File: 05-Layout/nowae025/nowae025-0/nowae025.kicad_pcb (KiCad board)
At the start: 2 copper layers, 17 parts, among them J1 JUMPER-2, J10 JUMPER-2, J11 JUMPER-2, J12 JUMPER-2, J13 JUMPER-2, J14 JUMPER-2, J2 JUMPER-2, J3 JUMPER-2, J4 JUMPER-2, J5 JUMPER-2, J6 JUMPER-2, J7 JUMPER-2, J8 JUMPER-2, J9 JUMPER-2, U1 BGM111A256V2

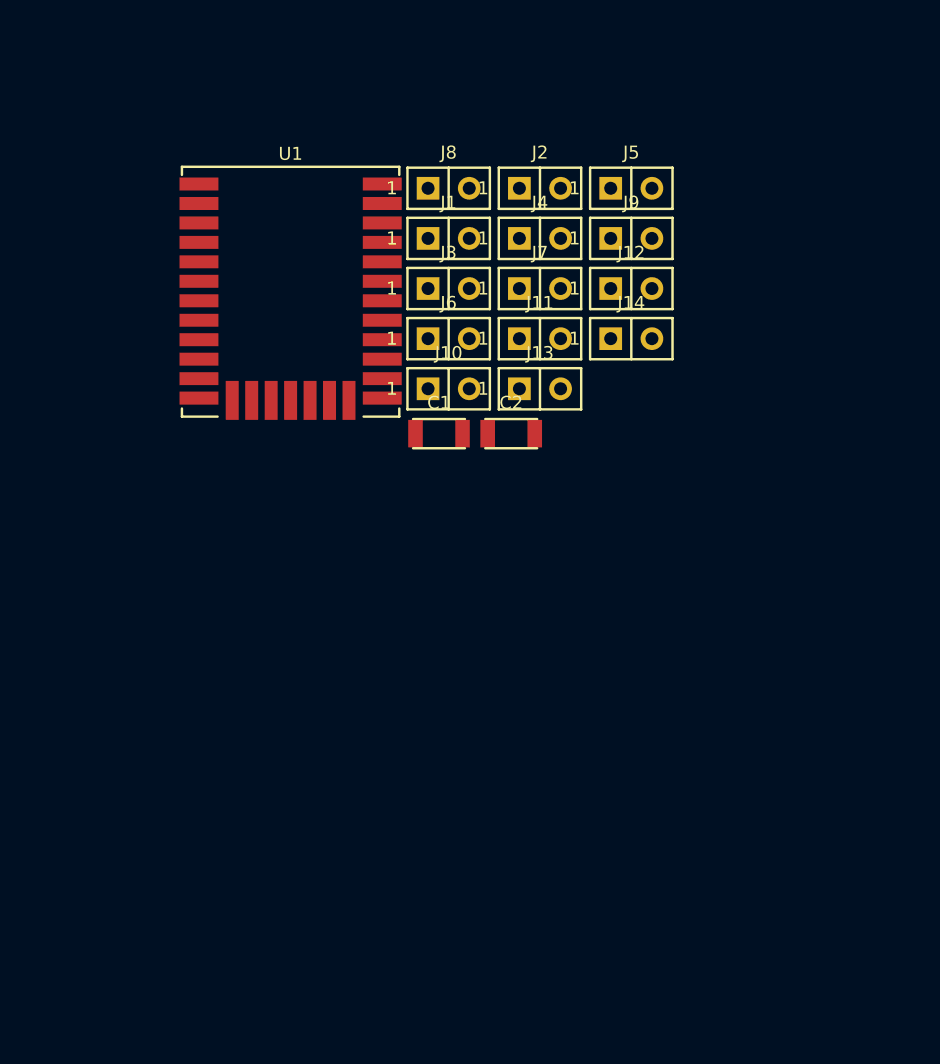
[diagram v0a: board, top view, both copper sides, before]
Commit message: Added missing footprint. Started component placement (nowae025)
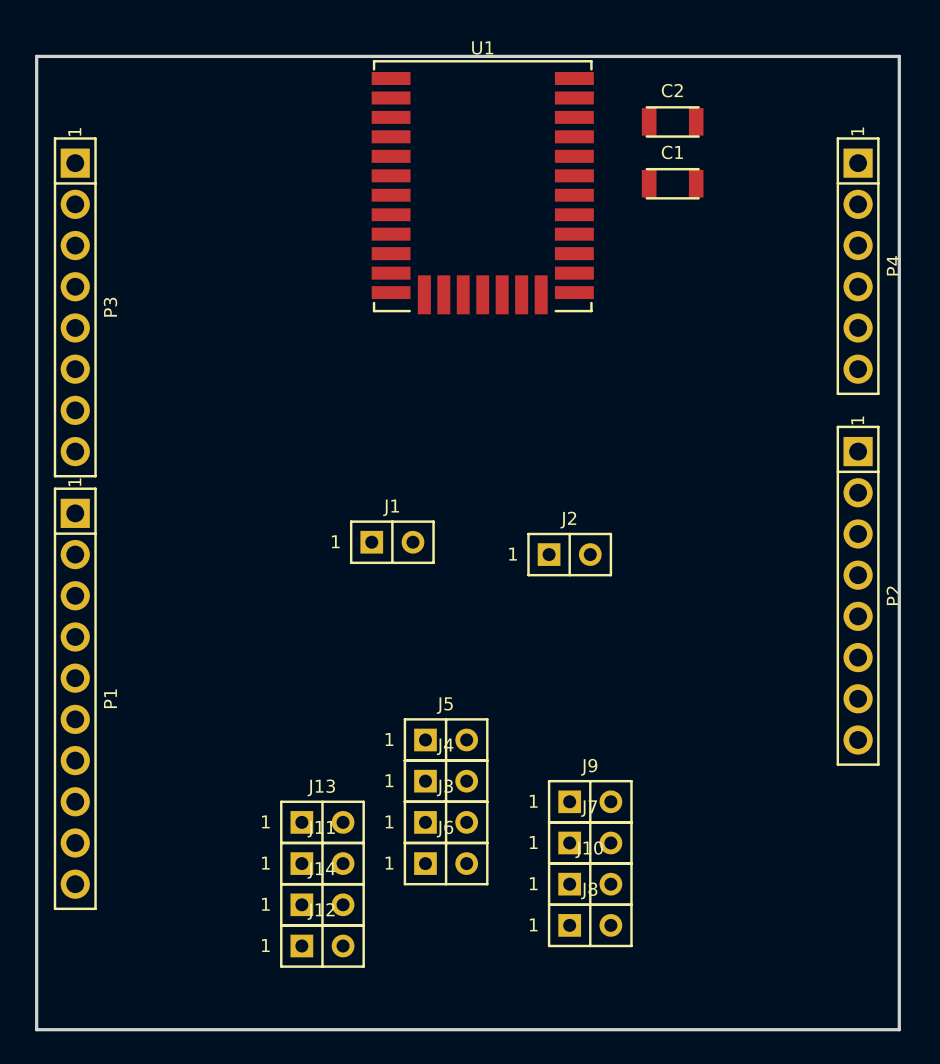
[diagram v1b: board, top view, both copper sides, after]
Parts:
- added P1: ARD_RIGHT2, CONNECTOR:SOCKET_10x1_2.54_WE-61301011821, F.Cu at (119.4, 101.6)
- added P2: ARD_LEFT2, CONNECTOR:SOCKET_8x1_2.54_WE-61300811821, F.Cu at (167.6, 95.2)
- added P3: ARD_RIGHT1, CONNECTOR:SOCKET_8x1_2.54_WE-61300811821, F.Cu at (119.4, 77.5)
- added P4: ARD_LEFT1, CONNECTOR:SOCKET_6x1_2.54_WE-61300611821, F.Cu at (167.6, 74.9)
- moved J8 46.3 mm to (151.1, 115.6)
- moved J12 44.8 mm to (134.6, 116.8)
- moved J14 39.8 mm to (134.6, 114.3)
- moved J5 35.9 mm to (142.2, 104.1)
- moved J11 35.0 mm to (134.6, 111.8)
- moved J9 34.8 mm to (151.1, 108.0)
- moved J7 34.3 mm to (151.1, 110.5)
- moved J4 34.0 mm to (142.2, 106.7)
- moved J3 32.9 mm to (142.2, 109.2)
- moved J6 32.4 mm to (142.2, 111.8)
- moved J10 31.8 mm to (151.1, 113.0)
- moved J13 29.9 mm to (134.6, 109.2)
- moved J2 22.7 mm to (149.9, 92.7)
- moved C2 21.6 mm to (156.2, 66.0)
- moved C1 21.1 mm to (156.2, 69.8)
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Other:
- board outline added: 53.2 x 60 mm

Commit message: Added testpoint and started routing (nowae025)
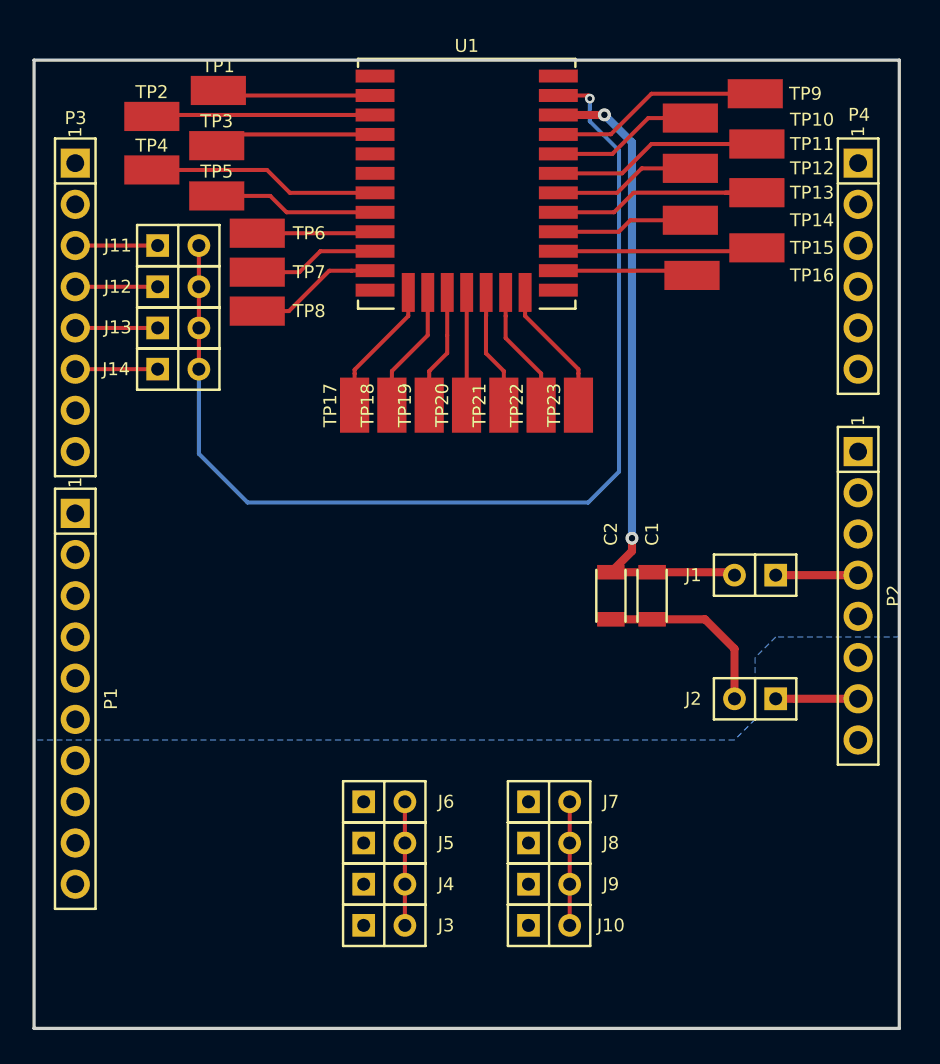
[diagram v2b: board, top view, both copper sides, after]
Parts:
- added TP1: TEST_POINT, MISC:TESTPOINT-KEYSTONE-5015, F.Cu at (128.2, 64.1)
- added TP10: TEST_POINT, MISC:TESTPOINT-KEYSTONE-5015, F.Cu at (157.3, 65.8)
- added TP11: TEST_POINT, MISC:TESTPOINT-KEYSTONE-5015, F.Cu at (161.4, 67.4)
- added TP12: TEST_POINT, MISC:TESTPOINT-KEYSTONE-5015, F.Cu at (157.3, 68.9)
- added TP13: TEST_POINT, MISC:TESTPOINT-KEYSTONE-5015, F.Cu at (161.4, 70.4)
- added TP14: TEST_POINT, MISC:TESTPOINT-KEYSTONE-5015, F.Cu at (157.3, 72.1)
- added TP15: TEST_POINT, MISC:TESTPOINT-KEYSTONE-5015, F.Cu at (161.4, 73.8)
- added TP16: TEST_POINT, MISC:TESTPOINT-KEYSTONE-5015, F.Cu at (157.4, 75.5)
- added TP17: TEST_POINT, MISC:TESTPOINT-KEYSTONE-5015, F.Cu at (136.6, 83.5)
- added TP18: TEST_POINT, MISC:TESTPOINT-KEYSTONE-5015, F.Cu at (138.9, 83.5)
- added TP19: TEST_POINT, MISC:TESTPOINT-KEYSTONE-5015, F.Cu at (141.2, 83.5)
- added TP2: TEST_POINT, MISC:TESTPOINT-KEYSTONE-5015, F.Cu at (124.1, 65.7)
- added TP20: TEST_POINT, MISC:TESTPOINT-KEYSTONE-5015, F.Cu at (143.5, 83.5)
- added TP21: TEST_POINT, MISC:TESTPOINT-KEYSTONE-5015, F.Cu at (145.8, 83.5)
- added TP22: TEST_POINT, MISC:TESTPOINT-KEYSTONE-5015, F.Cu at (148.1, 83.5)
- added TP23: TEST_POINT, MISC:TESTPOINT-KEYSTONE-5015, F.Cu at (150.4, 83.5)
- added TP3: TEST_POINT, MISC:TESTPOINT-KEYSTONE-5015, F.Cu at (128.1, 67.5)
- added TP4: TEST_POINT, MISC:TESTPOINT-KEYSTONE-5015, F.Cu at (124.1, 69.0)
- added TP5: TEST_POINT, MISC:TESTPOINT-KEYSTONE-5015, F.Cu at (128.1, 70.6)
- added TP6: TEST_POINT, MISC:TESTPOINT-KEYSTONE-5015, F.Cu at (130.6, 72.9)
- added TP7: TEST_POINT, MISC:TESTPOINT-KEYSTONE-5015, F.Cu at (130.6, 75.3)
- added TP8: TEST_POINT, MISC:TESTPOINT-KEYSTONE-5015, F.Cu at (130.6, 77.7)
- added TP9: TEST_POINT, MISC:TESTPOINT-KEYSTONE-5015, F.Cu at (161.3, 64.3)
- moved J12 41.6 mm to (125.7, 76.2)
- moved J11 39.1 mm to (125.7, 73.7)
- moved J14 34.2 mm to (125.7, 81.3)
- moved J13 31.8 mm to (125.7, 78.7)
- moved C2 29.5 mm to (152.4, 95.2), turned to 270 degrees
- moved C1 25.4 mm to (154.9, 95.2), turned to 270 degrees
- moved J1 22.5 mm to (161.3, 94.0), turned to 180 degrees
- moved J2 14.5 mm to (161.3, 101.6), turned to 180 degrees
- moved J3 7.41 mm to (138.4, 115.6)
- moved J4 7.41 mm to (138.4, 113.0)
- moved J5 7.41 mm to (138.4, 110.5)
- moved J8 5.68 mm to (148.6, 110.5)
- moved J9 5.68 mm to (148.6, 113.0)
- moved J6 5.39 mm to (138.4, 108.0)
- moved J10 3.59 mm to (148.6, 115.6)
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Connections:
- J10 pad 1: /ARDUINO_A5 -> /ARDUINO_A4
- J3 pad 1: /ARDUINO_D0 -> /ARDUINO_D1
- J4 pad 1: /ARDUINO_D14 -> /ARDUINO_D15
- J5 pad 1: /ARDUINO_A0 -> /ARDUINO_A1
- J6 pad 1: /ARDUINO_A4 -> /ARDUINO_A5
- J7 pad 1: /ARDUINO_D1 -> /ARDUINO_D0
- J8 pad 1: /ARDUINO_D15 -> /ARDUINO_D14
- J9 pad 1: /ARDUINO_A1 -> /ARDUINO_A0
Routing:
- net /BLE_RESET: track 0.00 -> 66.6 mm, vias 0 -> 1
- net +VDD: track 0.00 -> 40.0 mm, vias 0 -> 2
- net Net-(TP13-Pad1): track 0.00 -> 14.7 mm
- net Net-(TP4-Pad1): track 0.00 -> 14.3 mm
- net Net-(TP2-Pad1): track 0.00 -> 13.8 mm
- net Net-(TP9-Pad1): track 0.00 -> 13.2 mm
- net Net-(TP11-Pad1): track 0.00 -> 13.0 mm
- net Net-(TP15-Pad1): track 0.00 -> 12.3 mm
- net GND-ISO: track 0.00 -> 11.5 mm
- net Net-(TP5-Pad1): track 0.00 -> 10.2 mm
- net Net-(TP3-Pad1): track 0.00 -> 10.0 mm
- net Net-(TP1-Pad1): track 0.00 -> 9.79 mm
- net Net-(TP10-Pad1): track 0.00 -> 9.06 mm
- net Net-(TP12-Pad1): track 0.00 -> 8.77 mm
- net Net-(TP14-Pad1): track 0.00 -> 8.43 mm
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- added copper zone on B.Cu, net GND-ISO
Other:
- board size 53.2 x 60 mm -> 53.3 x 59.7 mm
- rule via_min_size: 0.4 -> 0.6
